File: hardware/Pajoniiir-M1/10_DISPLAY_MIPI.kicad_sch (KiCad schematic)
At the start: 30 parts

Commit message: hardware: bind remaining hierarchical ports to nets
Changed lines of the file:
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@@
   (junction (at 189.865 85.09) (diameter 0) (color 0 0 0 0))
   (hierarchical_label "3V3_SYS" (shape input) (at 29.845 29.845 0) (effects (font (size 1.27 1.27))))
-  (hierarchical_label "5V_SYS" (shape input) (at 29.845 34.925 0) (effects (font (size 1.27 1.27))))
-  (hierarchical_label "P4_LDO_MIPI_2V5" (shape input) (at 29.845 40.005 0) (effects (font (size 1.27 1.27))))
+  (hierarchical_label "5V_SYS" (shape input) (at 154.94 29.845 0) (effects (font (size 1.27 1.27))))
+  (hierarchical_label "P4_LDO_MIPI_2V5" (shape input) (at 125.095 40.005 0) (effects (font (size 1.27 1.27))))
   (symbol
     (lib_id "Device:R_US") (at 55.245 29.845 90) (unit 1)
@@
     (instances (project "Pajoniiir-M1" (path "/2c8dd352-b7b8-4d9e-8f93-5dd43be2a100/3100000a-6b2a-4a3a-8c91-00000000000a" (reference "TP_MIPI_2V5") (unit 1))))
   )
-  (label "P4_LDO_MIPI_2V5" (at 125.095 40.005 0) (effects (font (size 1.27 1.27))))
   (hierarchical_label "DSI_D0_P" (shape bidirectional) (at 29.845 55.245 0) (effects (font (size 1.27 1.27))))
   (symbol
@@
     (instances (project "Pajoniiir-M1" (path "/2c8dd352-b7b8-4d9e-8f93-5dd43be2a100/3100000a-6b2a-4a3a-8c91-00000000000a" (reference "C_BL_IN") (unit 1))))
   )
-  (label "5V_SYS" (at 154.94 29.845 0) (effects (font (size 1.27 1.27))))
   (symbol
     (lib_id "power:GND") (at 154.94 37.465 0) (unit 1)

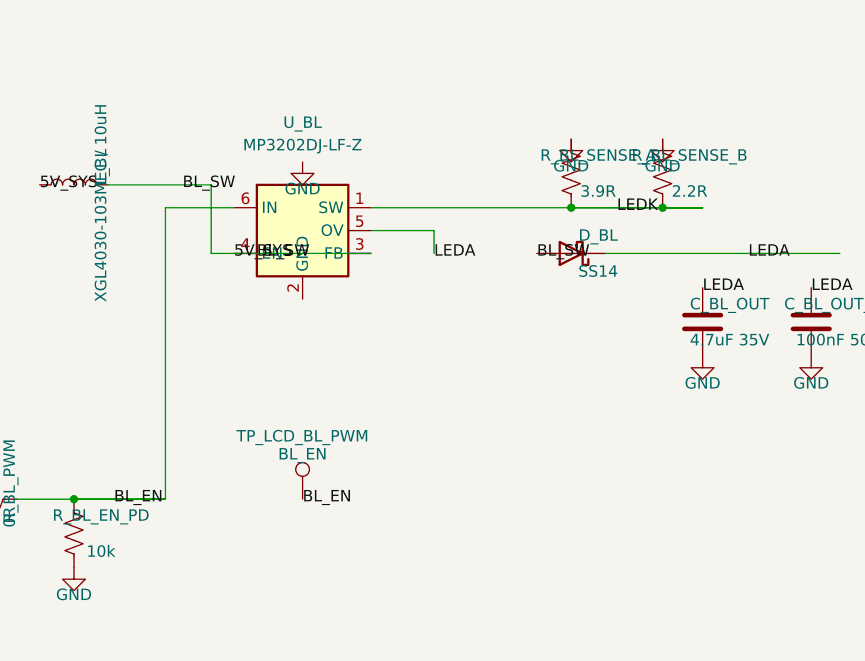
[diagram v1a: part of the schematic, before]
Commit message: hardware: correct MP3202 backlight pin mapping
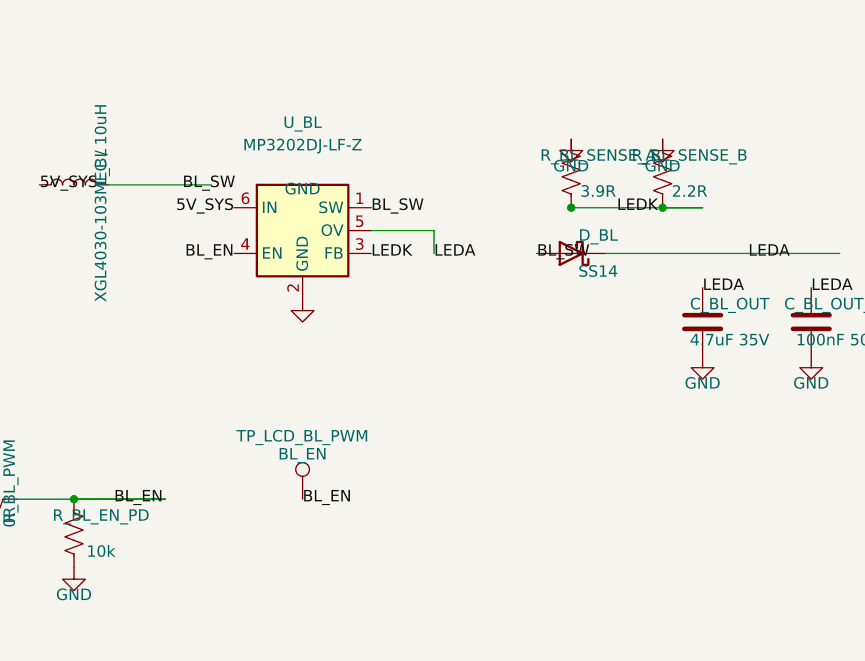
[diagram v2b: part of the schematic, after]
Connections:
- net 5V_SYS: now also U_BL.6 (IN); no longer D_BL.2 (A), L_BL.2, U_BL.3 (FB), U_BL.4 (EN)
- net BL_EN: now also U_BL.4 (EN); no longer U_BL.6 (IN)
- net GND: now also U_BL.2 (GND)
- net LEDK: now also U_BL.3 (FB); no longer U_BL.1 (SW)
- new net BL_SW: D_BL.2 (A), L_BL.2, U_BL.1 (SW)
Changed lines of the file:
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@@
     (comment 2 "J_LCD physical pinout/footprint remains hard-gated pending authoritative panel/FPC")
   )
+  (label "LEDK" (at 222.885 57.785 0) (effects (font (size 1.27 1.27))))
+  (label "BL_EN" (at 207.645 57.785 180) (effects (font (size 1.27 1.27))))
   (junction (at 90.17 111.76) (diameter 0) (color 0 0 0 0))
   (junction (at 245.11 52.705) (diameter 0) (color 0 0 0 0))
@@
     (instances (project "Pajoniiir-M1" (path "/2c8dd352-b7b8-4d9e-8f93-5dd43be2a100/3100000a-6b2a-4a3a-8c91-00000000000a" (reference "U_BL") (unit 1))))
   )
-  (wire (pts (xy 205.105 50.165) (xy 205.105 57.785)) (stroke (width 0) (type default)))
-  (wire (pts (xy 205.105 57.785) (xy 222.885 57.785)) (stroke (width 0) (type default)))
-  (label "BL_SW" (at 210.185 57.785 0) (effects (font (size 1.27 1.27))))
-  (label "5V_SYS" (at 207.645 57.785 0) (effects (font (size 1.27 1.27))))
-  (symbol
-    (lib_id "power:GND") (at 215.265 47.625 0) (unit 1)
+  (label "BL_SW" (at 222.885 52.705 0) (effects (font (size 1.27 1.27))))
+  (label "5V_SYS" (at 207.645 52.705 180) (effects (font (size 1.27 1.27))))
+  (symbol
+    (lib_id "power:GND") (at 215.265 62.865 0) (unit 1)
     (exclude_from_sim no) (in_bom yes) (on_board yes) (dnp no)
     (property "Reference" "#PWR1006" (at 215.265 53.625 0) (effects (font (size 1.27 1.27)) (hide yes)))
@@
   )
   (label "LEDA" (at 290.195 57.785 0) (effects (font (size 1.27 1.27))))
-  (wire (pts (xy 222.885 52.705) (xy 259.715 52.705)) (stroke (width 0) (type default)))
   (label "LEDK" (at 250.19 52.705 0) (effects (font (size 1.27 1.27))))
   (symbol
@@
   (wire (pts (xy 149.86 85.09) (xy 175.895 85.09)) (stroke (width 0) (type default)))
   (wire (pts (xy 183.515 85.09) (xy 200.025 85.09)) (stroke (width 0) (type default)))
-  (wire (pts (xy 200.025 85.09) (xy 200.025 52.705)) (stroke (width 0) (type default)))
-  (wire (pts (xy 200.025 52.705) (xy 207.645 52.705)) (stroke (width 0) (type default)))
   (label "BL_EN" (at 194.31 85.09 0) (effects (font (size 1.27 1.27))))
   (symbol

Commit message: hardware: normalize endpoint nets and fix microSD input rail
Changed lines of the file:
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@@
   (wire (pts (xy 29.845 55.245) (xy 55.88 55.245)) (stroke (width 0) (type default)))
   (wire (pts (xy 63.5 55.245) (xy 114.935 55.245)) (stroke (width 0) (type default)))
-  (label "PANEL_DSI_D0_P" (at 90.17 55.245 0) (effects (font (size 1.27 1.27))))
+  (label "PANEL_DSI_D0_P" (at 63.5 55.245 0) (effects (font (size 1.27 1.27))))
   (hierarchical_label "DSI_D0_N" (shape bidirectional) (at 29.845 62.23 0) (effects (font (size 1.27 1.27))))
   (symbol
@@
   (wire (pts (xy 29.845 62.23) (xy 55.88 62.23)) (stroke (width 0) (type default)))
   (wire (pts (xy 63.5 62.23) (xy 114.935 62.23)) (stroke (width 0) (type default)))
-  (label "PANEL_DSI_D0_N" (at 90.17 62.23 0) (effects (font (size 1.27 1.27))))
+  (label "PANEL_DSI_D0_N" (at 63.5 62.23 0) (effects (font (size 1.27 1.27))))
   (hierarchical_label "DSI_D1_P" (shape bidirectional) (at 29.845 73.025 0) (effects (font (size 1.27 1.27))))
   (symbol
@@
   (wire (pts (xy 29.845 73.025) (xy 55.88 73.025)) (stroke (width 0) (type default)))
   (wire (pts (xy 63.5 73.025) (xy 114.935 73.025)) (stroke (width 0) (type default)))
-  (label "PANEL_DSI_D1_P" (at 90.17 73.025 0) (effects (font (size 1.27 1.27))))
+  (label "PANEL_DSI_D1_P" (at 63.5 73.025 0) (effects (font (size 1.27 1.27))))
   (hierarchical_label "DSI_D1_N" (shape bidirectional) (at 29.845 80.01 0) (effects (font (size 1.27 1.27))))
   (symbol
@@
   (wire (pts (xy 29.845 80.01) (xy 55.88 80.01)) (stroke (width 0) (type default)))
   (wire (pts (xy 63.5 80.01) (xy 114.935 80.01)) (stroke (width 0) (type default)))
-  (label "PANEL_DSI_D1_N" (at 90.17 80.01 0) (effects (font (size 1.27 1.27))))
+  (label "PANEL_DSI_D1_N" (at 63.5 80.01 0) (effects (font (size 1.27 1.27))))
   (hierarchical_label "DSI_CLK_P" (shape bidirectional) (at 29.845 90.805 0) (effects (font (size 1.27 1.27))))
   (symbol
@@
   (wire (pts (xy 29.845 90.805) (xy 55.88 90.805)) (stroke (width 0) (type default)))
   (wire (pts (xy 63.5 90.805) (xy 114.935 90.805)) (stroke (width 0) (type default)))
-  (label "PANEL_DSI_CLK_P" (at 90.17 90.805 0) (effects (font (size 1.27 1.27))))
+  (label "PANEL_DSI_CLK_P" (at 63.5 90.805 0) (effects (font (size 1.27 1.27))))
   (hierarchical_label "DSI_CLK_N" (shape bidirectional) (at 29.845 97.79 0) (effects (font (size 1.27 1.27))))
   (symbol
@@
   (wire (pts (xy 29.845 97.79) (xy 55.88 97.79)) (stroke (width 0) (type default)))
   (wire (pts (xy 63.5 97.79) (xy 114.935 97.79)) (stroke (width 0) (type default)))
-  (label "PANEL_DSI_CLK_N" (at 90.17 97.79 0) (effects (font (size 1.27 1.27))))
+  (label "PANEL_DSI_CLK_N" (at 63.5 97.79 0) (effects (font (size 1.27 1.27))))
   (hierarchical_label "LCD_RST" (shape input) (at 29.845 111.76 0) (effects (font (size 1.27 1.27))))
   (symbol
